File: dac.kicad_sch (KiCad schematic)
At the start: 68 parts, among them J16 3.5mm_Jack, J9 3.5mm_Jack, Q2 FMMT591, Q3 FMMT491, Q4 FMMT491, Q5 FMMT591, U1 CJC4334H, U9 OPA1612AxD

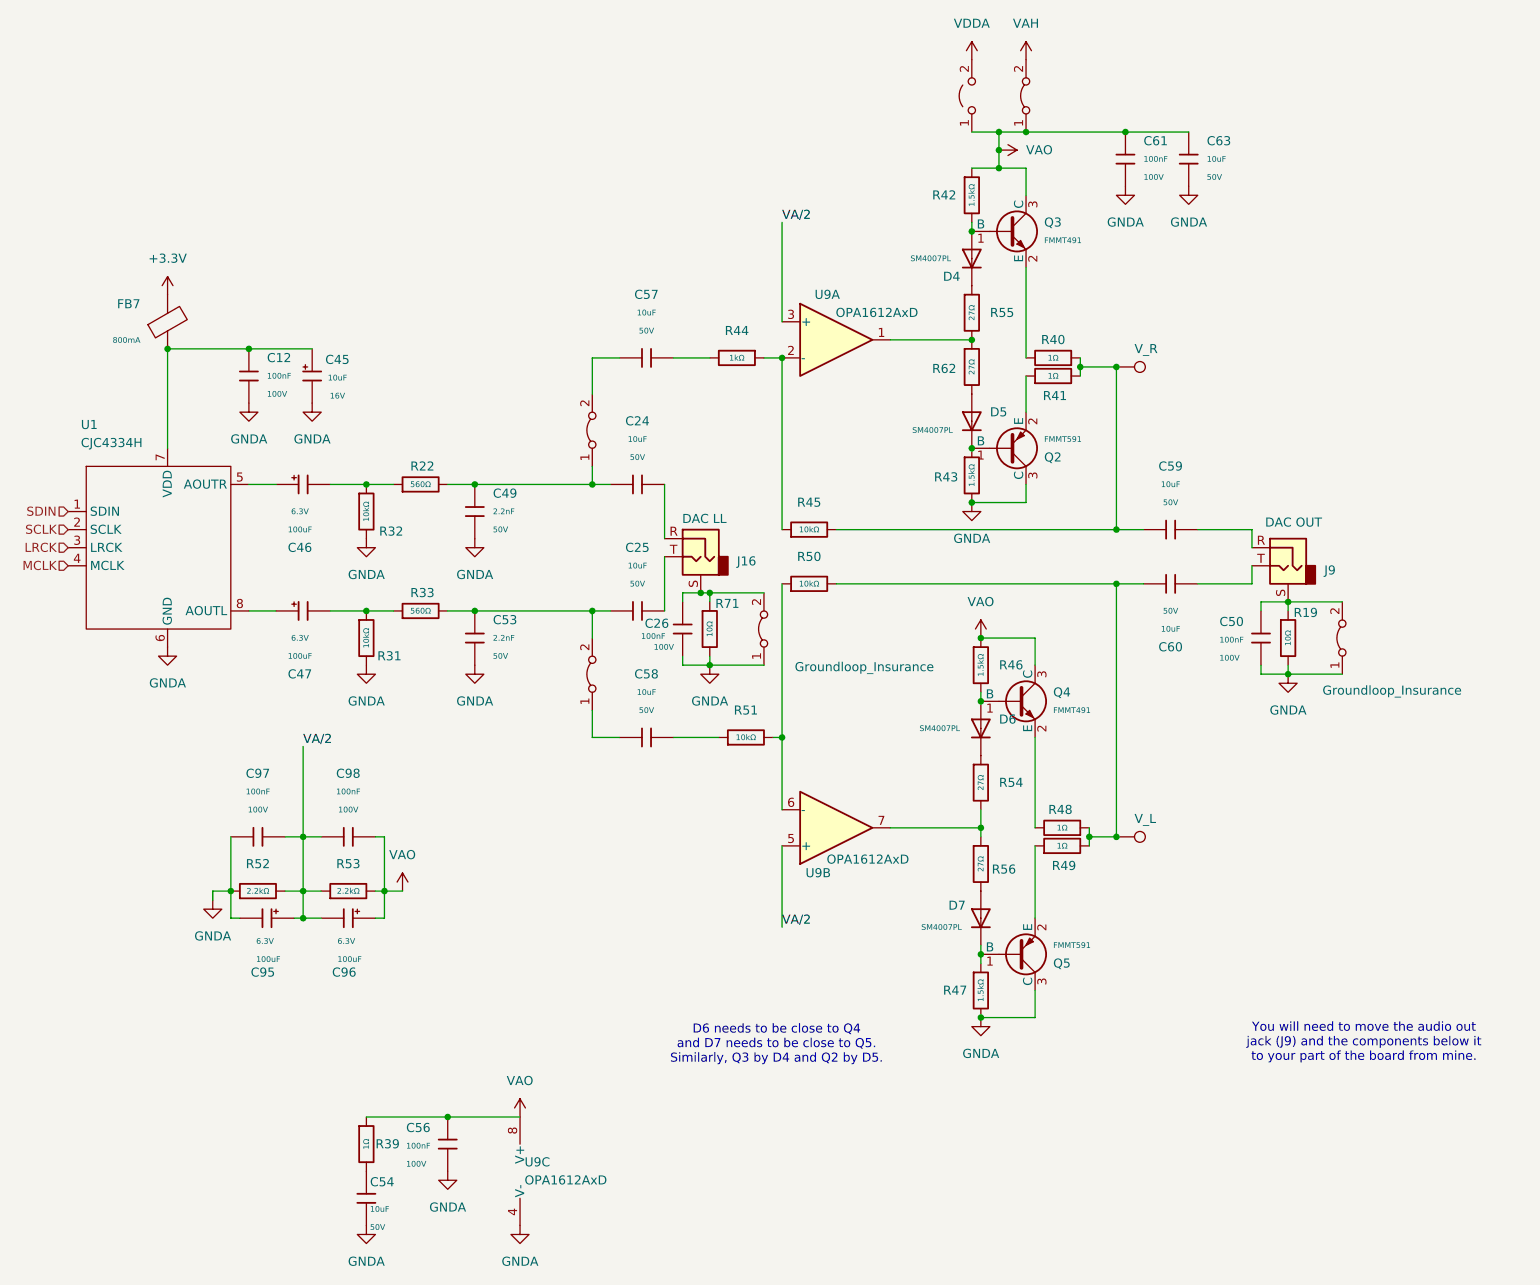
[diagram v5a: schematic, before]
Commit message: Changed push pull to PAM8908
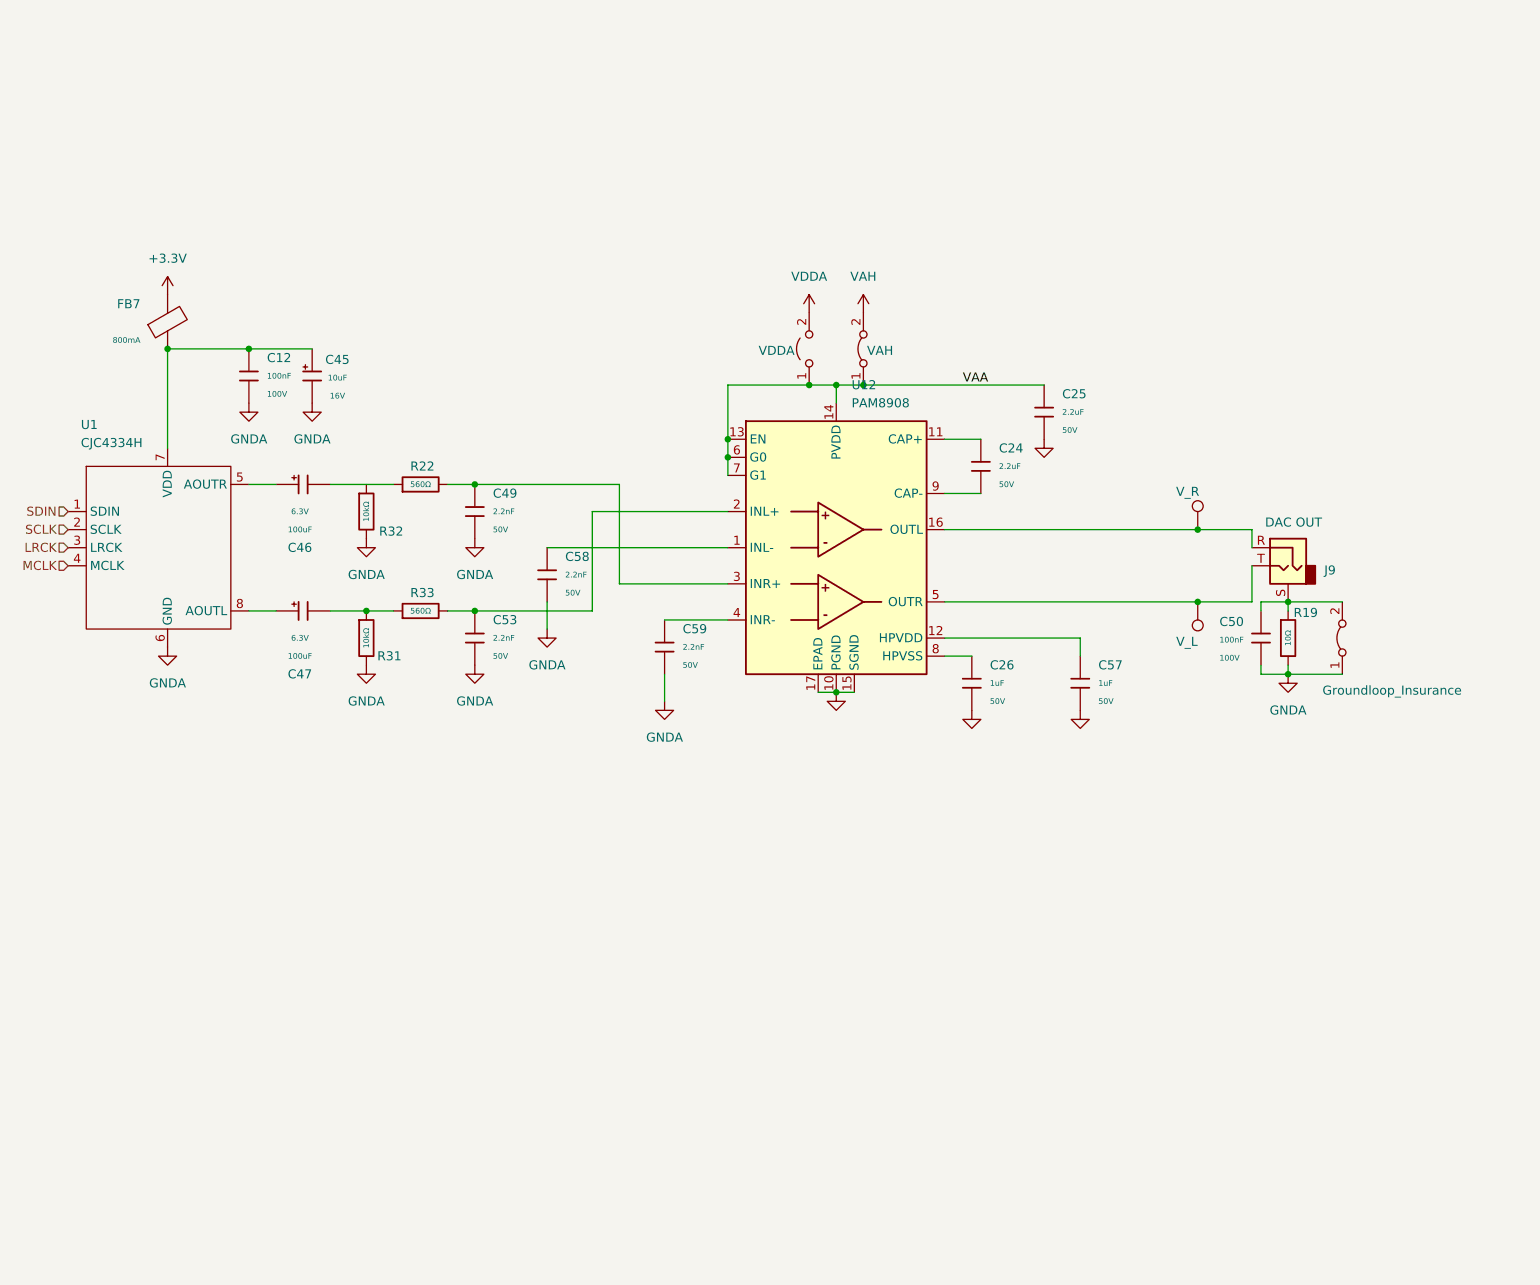
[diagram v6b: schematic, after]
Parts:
- removed C24, C25, C57, C58, C59, C60, C63: 10uF, PCM_JLCPCB:C_0805, symbol PCM_JLCPCB-Capacitors:0805,10uF,(2)
- removed C26, C56, C61, C97, C98: 100nF, PCM_JLCPCB:C_0805, symbol PCM_JLCPCB-Capacitors:0805,100nF
- removed C54: 10uF, PCM_JLCPCB:C_1206, symbol PCM_JLCPCB-Capacitors:1206,10uF
- removed C95, C96: 100uF, PCM_JLCPCB:C_CASE-B-3528-21(mm), symbol PCM_JLCPCB-Capacitors:CASE-B-3528-21(mm),100uF
- removed D4, D5, D6, D7: SM4007PL, PCM_JLCPCB:D_SOD-123FL, symbol PCM_JLCPCB-Diodes:General,SM4007PL
- removed J16: 3.5mm_Jack, Intro_to_CAD:Jack_3.5mm_CUI_SJ-3523-SMT_Horizontal, symbol Connector_Audio:AudioJack2_Ground
- removed Q2, Q5: FMMT591, PCM_JLCPCB:Q_SOT-23, symbol PCM_JLCPCB-Transistors:PNP,FMMT591
- removed Q3, Q4: FMMT491, PCM_JLCPCB:Q_SOT-23, symbol PCM_JLCPCB-Transistors:NPN,FMMT491
- removed R39, R40, R41, R48, R49: 1Ω, PCM_JLCPCB:R_0805, symbol PCM_JLCPCB-Resistors:0805,1Ω
- removed R42, R43, R46, R47: 1.5kΩ, PCM_JLCPCB:R_0805, symbol PCM_JLCPCB-Resistors:0805,1.5kΩ
- removed R44: 1kΩ, PCM_JLCPCB:R_0805, symbol PCM_JLCPCB-Resistors:0805,1kΩ
- removed R45, R50, R51: 10kΩ, PCM_JLCPCB:R_0805, symbol PCM_JLCPCB-Resistors:0805,10kΩ
- removed R52, R53: 2.2kΩ, PCM_JLCPCB:R_0805, symbol PCM_JLCPCB-Resistors:0805,2.2kΩ
- removed R54, R55, R56, R62: 27Ω, PCM_JLCPCB:R_0805, symbol PCM_JLCPCB-Resistors:0805,27Ω
- removed R71: 10Ω, PCM_JLCPCB:R_0603, symbol PCM_JLCPCB-Resistors:0603,10Ω
- removed U9: OPA1612AxD, Package_SO:SOIC-8_3.9x4.9mm_P1.27mm, symbol Amplifier_Operational:OPA1612AxD
- removed e6, e7: (no value), Jumper:SolderJumper-2_P1.3mm_Bridged_RoundedPad1.0x1.5mm, symbol Jumper:Jumper_2_Bridged
- removed e8: Groundloop_Insurance, Jumper:SolderJumper-2_P1.3mm_Bridged_RoundedPad1.0x1.5mm, symbol Jumper:Jumper_2_Bridged
- added C24, C25: 2.2uF, PCM_JLCPCB:C_0805, symbol PCM_JLCPCB-Capacitors:0805,2.2uF
- added C26, C57: 1uF, PCM_JLCPCB:C_0805, symbol PCM_JLCPCB-Capacitors:0805,1uF
- added C58, C59: 2.2nF, PCM_JLCPCB:C_0805, symbol PCM_JLCPCB-Capacitors:0805,2.2nF
- added U12: PAM8908, Package_DFN_QFN:QFN-16-1EP_3x3mm_P0.5mm_EP1.7x1.7mm, symbol Amplifier_Audio:PAM8908
- JP3: value (none) -> VDDA
- e2: value (none) -> VAH
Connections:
- net GNDA: now also C25.2, C26.2, C57.2, C58.2, C59.2, U12.10 (PGND), U12.15 (SGND), U12.17 (EPAD)
- net at TP9.1: now also J9.T, U12.5 (OUTR)
- net at J9.R: now also TP8.1, U12.16 (OUTL)
- net at C49.1, R22.2: now also U12.3 (INR+)
- net at C53.1, R33.2: now also U12.2 (INL+)
- net at C46.2, R22.1: no longer R32.1
- net VAO renamed VAA
- net VAA: now also C25.1, U12.13 (EN), U12.14 (PVDD), U12.6 (G0), U12.7 (G1)
- new net: C24.1, U12.11 (CAP+)
- new net: C24.2, U12.9 (CAP-)
- new net: C59.1, U12.4 (INR-)
- new net: C58.1, U12.1 (INL-)
- new net: C57.1, U12.12 (HPVDD)
- new net: C26.1, U12.8 (HPVSS)
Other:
- note removed: "D6 needs to be close to Q4 and D7 needs to be close to Q5. Similarly, Q3 by D4 and Q2 by D5."
- note removed: "You will need to move the audio out jack (J9) and the components below it to your part of the board from mine."

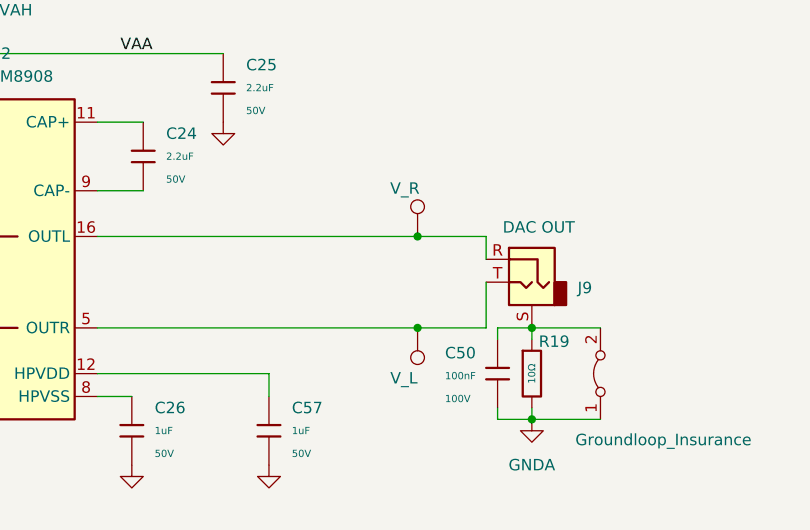
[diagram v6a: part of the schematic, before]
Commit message: Fixed CJC5340 C Number
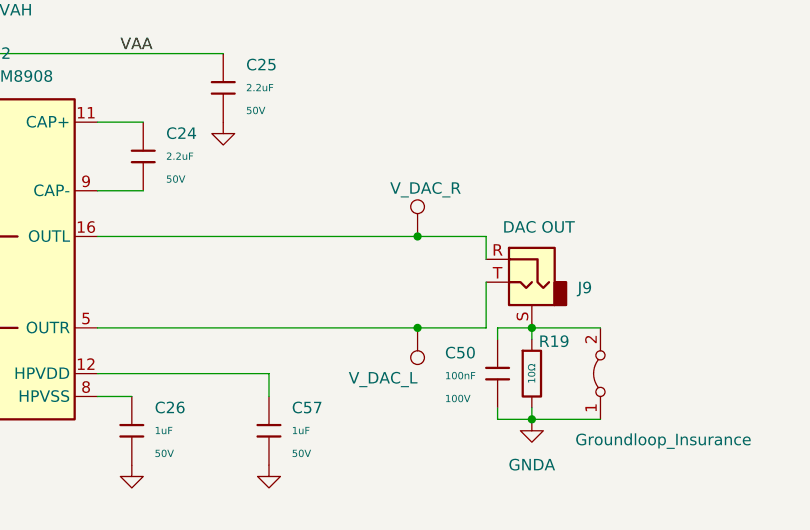
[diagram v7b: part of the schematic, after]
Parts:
- TP8: value V_R -> V_DAC_R
- TP9: value V_L -> V_DAC_L
- U12: LCSC C55513 -> C33233
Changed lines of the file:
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@@
 			)
 		)
-		(property "LCSC" "C55513"
+		(property "LCSC" "C33233"
 			(at 165.1 87.63 0)
 			(hide yes)
@@
 			)
 		)
-		(property "Value" "V_L"
+		(property "Value" "V_DAC_L"
 			(at 215.9 100.838 0)
 			(show_name no)
@@
 			)
 		)
-		(property "Value" "V_R"
+		(property "Value" "V_DAC_R"
 			(at 212.852 79.756 0)
 			(show_name no)
